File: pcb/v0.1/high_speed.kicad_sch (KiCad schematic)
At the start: 14 parts, among them J1 USB_C_Receptacle_fw, J2 USB_C_Receptacle_fw, J22 690-019-298-412, J5 Conn_01x22_Female, U12 RT9742SNGV, U6 AP22653W6

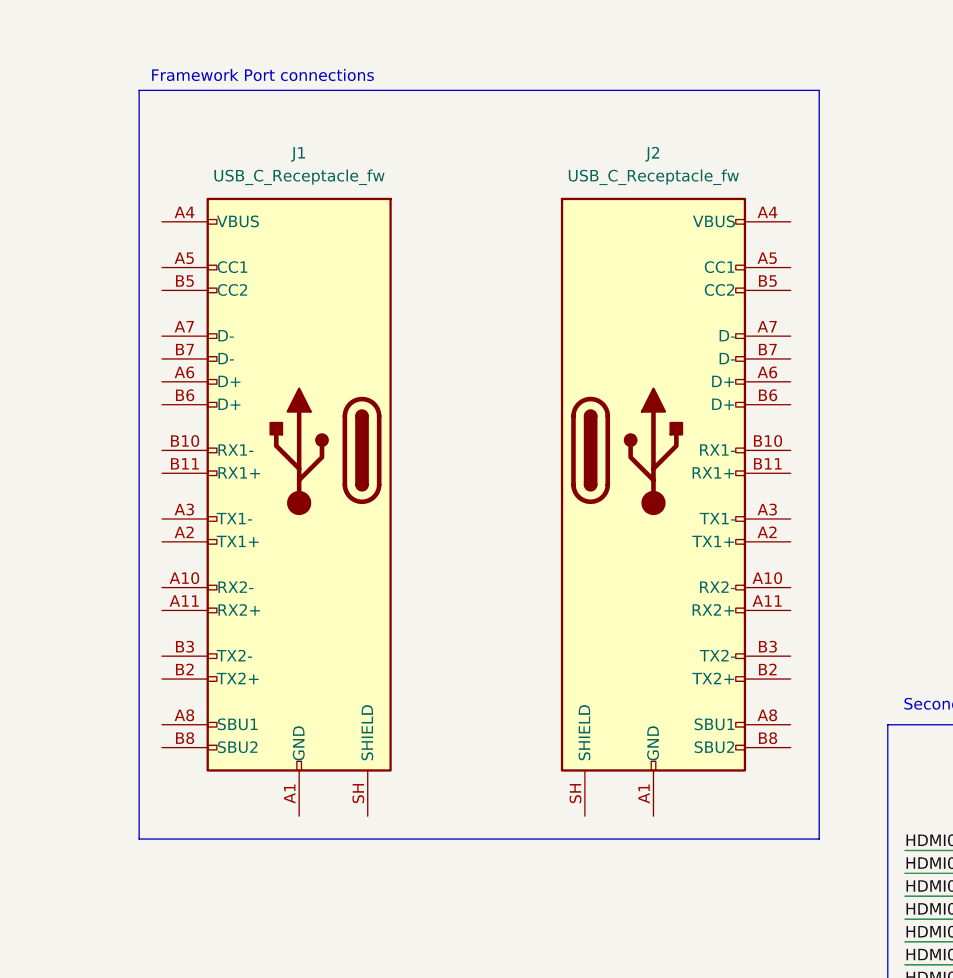
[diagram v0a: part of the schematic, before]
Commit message: Add co processor as its own sub page
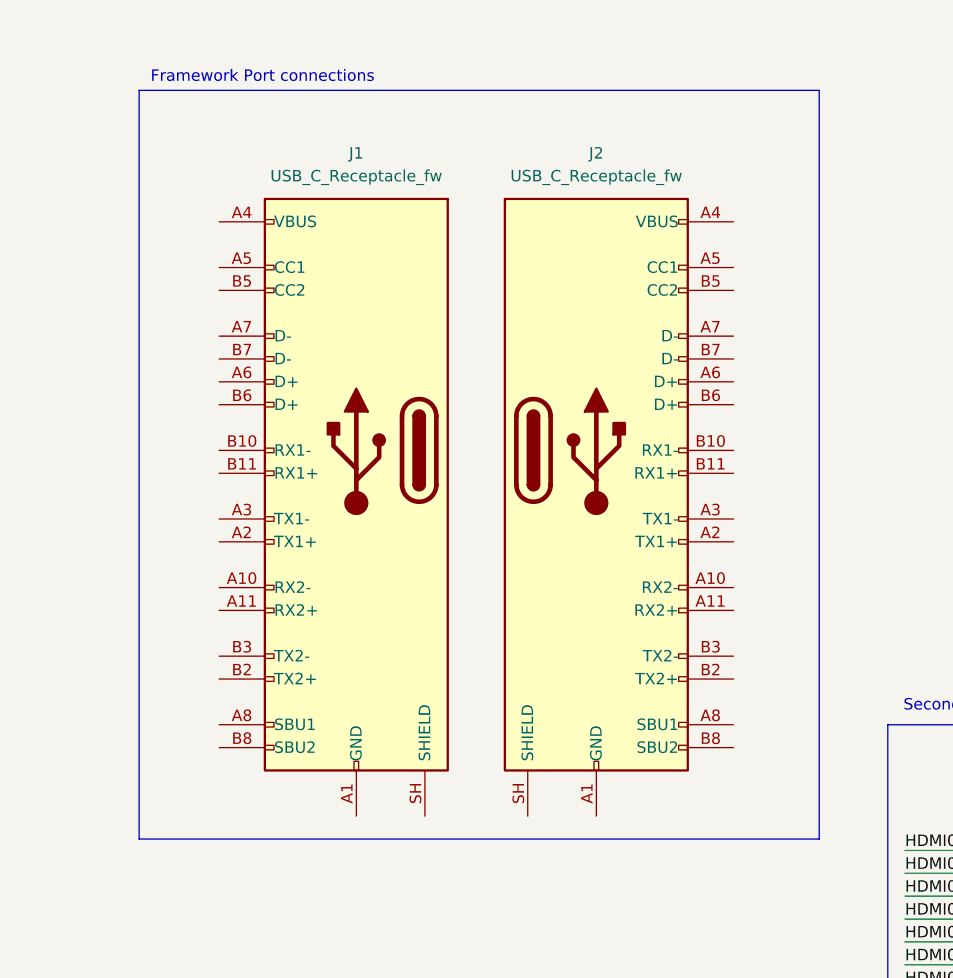
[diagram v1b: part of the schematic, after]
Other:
- moved on the sheet: J1, J2
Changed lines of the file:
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@@
 	(symbol
 		(lib_id "TH-1-CC:USB_C_Receptacle_fw")
-		(at 161.29 60.96 0)
+		(at 167.64 60.96 0)
 		(mirror y)
 		(unit 1)
@@
 		(dnp no)
 		(property "Reference" "J1"
-			(at 161.29 27.94 0)
+			(at 167.64 27.94 0)
 			(show_name no)
 			(do_not_autoplace no)
@@
 		)
 		(property "Value" "USB_C_Receptacle_fw"
-			(at 161.29 30.48 0)
+			(at 167.64 30.48 0)
 			(show_name no)
 			(do_not_autoplace no)
@@
 		)
 		(property "Footprint" ""
-			(at 157.48 60.96 0)
+			(at 163.83 60.96 0)
 			(hide yes)
 			(show_name no)
@@
 		)
 		(property "Datasheet" "https://gct.co/files/specs/usb4056-spec.pdf"
-			(at 157.48 60.96 0)
+			(at 163.83 60.96 0)
 			(hide yes)
 			(show_name no)
@@
 		)
 		(property "Description" "USB Full-Featured Type-C Receptacle connector"
-			(at 161.29 60.96 0)
+			(at 167.64 60.96 0)
 			(hide yes)
 			(show_name no)
@@
 		)
 		(property "Manufacturer" "GCT"
-			(at 161.29 60.96 0)
+			(at 167.64 60.96 0)
 			(hide yes)
 			(show_name no)
@@
 		)
 		(property "Mfr. Part no" "USB4056-03-A"
-			(at 161.29 60.96 0)
+			(at 167.64 60.96 0)
 			(hide yes)
 			(show_name no)
@@
 		)
 		(property "Distributor Digikey" "https://www.digikey.co.uk/en/products/detail/gct/USB4056-03-A/14638038"
-			(at 161.29 60.96 0)
+			(at 167.64 60.96 0)
 			(hide yes)
 			(show_name no)
@@
 		)
 		(property "Digikey Part no" "2073-USB4056-03-ATR-ND"
-			(at 161.29 60.96 0)
+			(at 167.64 60.96 0)
 			(hide yes)
 			(show_name no)
@@
 		)
 		(property "Stock" "NO!"
-			(at 161.29 60.96 0)
+			(at 167.64 60.96 0)
 			(hide yes)
 			(show_name no)
@@
 	(symbol
 		(lib_id "TH-1-CC:USB_C_Receptacle_fw")
-		(at 200.66 60.96 0)
+		(at 194.31 60.96 0)
 		(unit 1)
 		(body_style 1)
@@
 		(fields_autoplaced yes)
 		(property "Reference" "J2"
-			(at 200.66 27.94 0)
+			(at 194.31 27.94 0)
 			(show_name no)
 			(do_not_autoplace no)
@@
 		)
 		(property "Value" "USB_C_Receptacle_fw"
-			(at 200.66 30.48 0)
+			(at 194.31 30.48 0)
 			(show_name no)
 			(do_not_autoplace no)
@@
 		)
 		(property "Footprint" ""
-			(at 204.47 60.96 0)
+			(at 198.12 60.96 0)
 			(hide yes)
 			(show_name no)
@@
 		)
 		(property "Datasheet" "https://gct.co/files/specs/usb4056-spec.pdf"
-			(at 204.47 60.96 0)
+			(at 198.12 60.96 0)
 			(hide yes)
 			(show_name no)
@@
 		)
 		(property "Description" "USB Full-Featured Type-C Receptacle connector"
-			(at 200.66 60.96 0)
+			(at 194.31 60.96 0)
 			(hide yes)
 			(show_name no)
@@
 		)
 		(property "Manufacturer" "GCT"
-			(at 200.66 60.96 0)
+			(at 194.31 60.96 0)
 			(hide yes)
 			(show_name no)
@@
 		)
 		(property "Mfr. Part no" "USB4056-03-A"
-			(at 200.66 60.96 0)
+			(at 194.31 60.96 0)
 			(hide yes)
 			(show_name no)
@@
 		)
 		(property "Distributor Digikey" "https://www.digikey.co.uk/en/products/detail/gct/USB4056-03-A/14638038"
-			(at 200.66 60.96 0)
+			(at 194.31 60.96 0)
 			(hide yes)
 			(show_name no)
@@
 		)
 		(property "Digikey Part no" "2073-USB4056-03-ATR-ND"
-			(at 200.66 60.96 0)
+			(at 194.31 60.96 0)
 			(hide yes)
 			(show_name no)
@@
 		)
 		(property "Stock" "NO!"
-			(at 200.66 60.96 0)
-			(hide yes)
-			(show_name no)
+			(at 194.31 60.96 0)
+			(hide yes)
+			(show_name no)

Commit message: Add IR subsystem to schematic + clean up layout
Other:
- company: (none) -> Teahaz Computer
- title: (none) -> TH-1 Mainbaord devkit: High speed components
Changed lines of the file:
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@@
 	(generator_version "10.0")
 	(paper "A4")
+	(title_block
+		(title "TH-1 Mainbaord devkit: High speed components")
+		(date "2026-05-29")
+		(rev "0.1")
+		(company "Teahaz Computer")
+	)
 	(rectangle
 		(start 143.51 20.955)

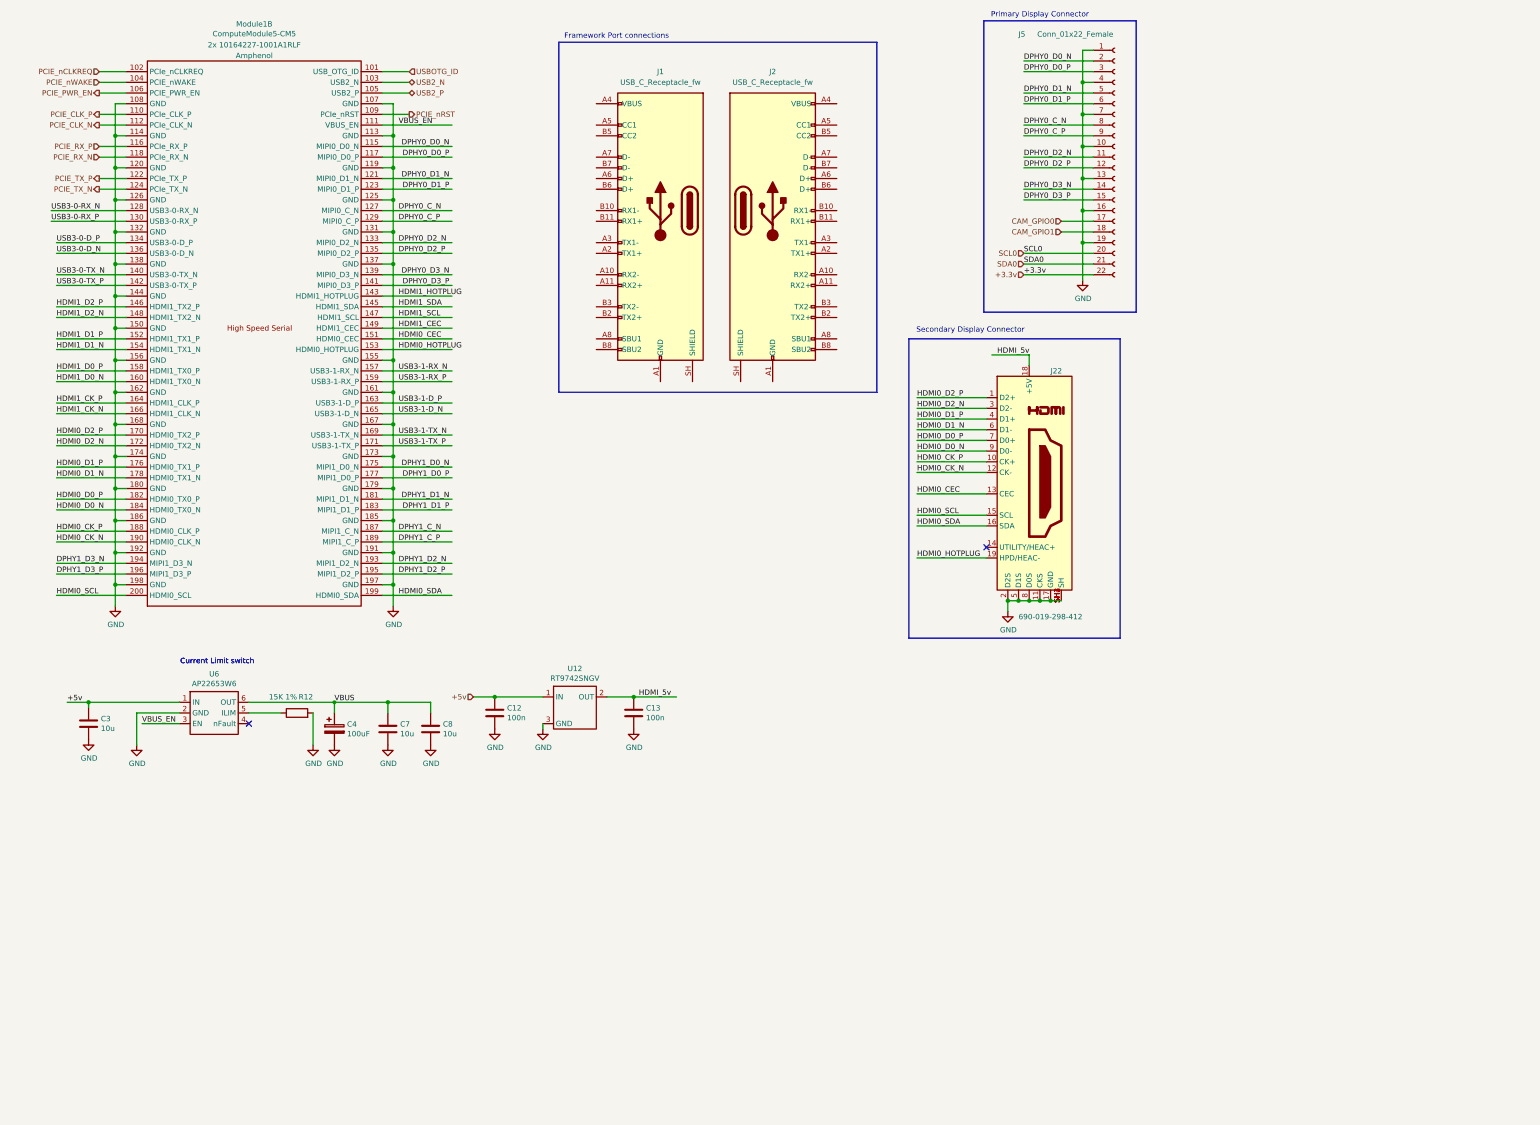
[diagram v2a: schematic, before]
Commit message: More work on the sound system
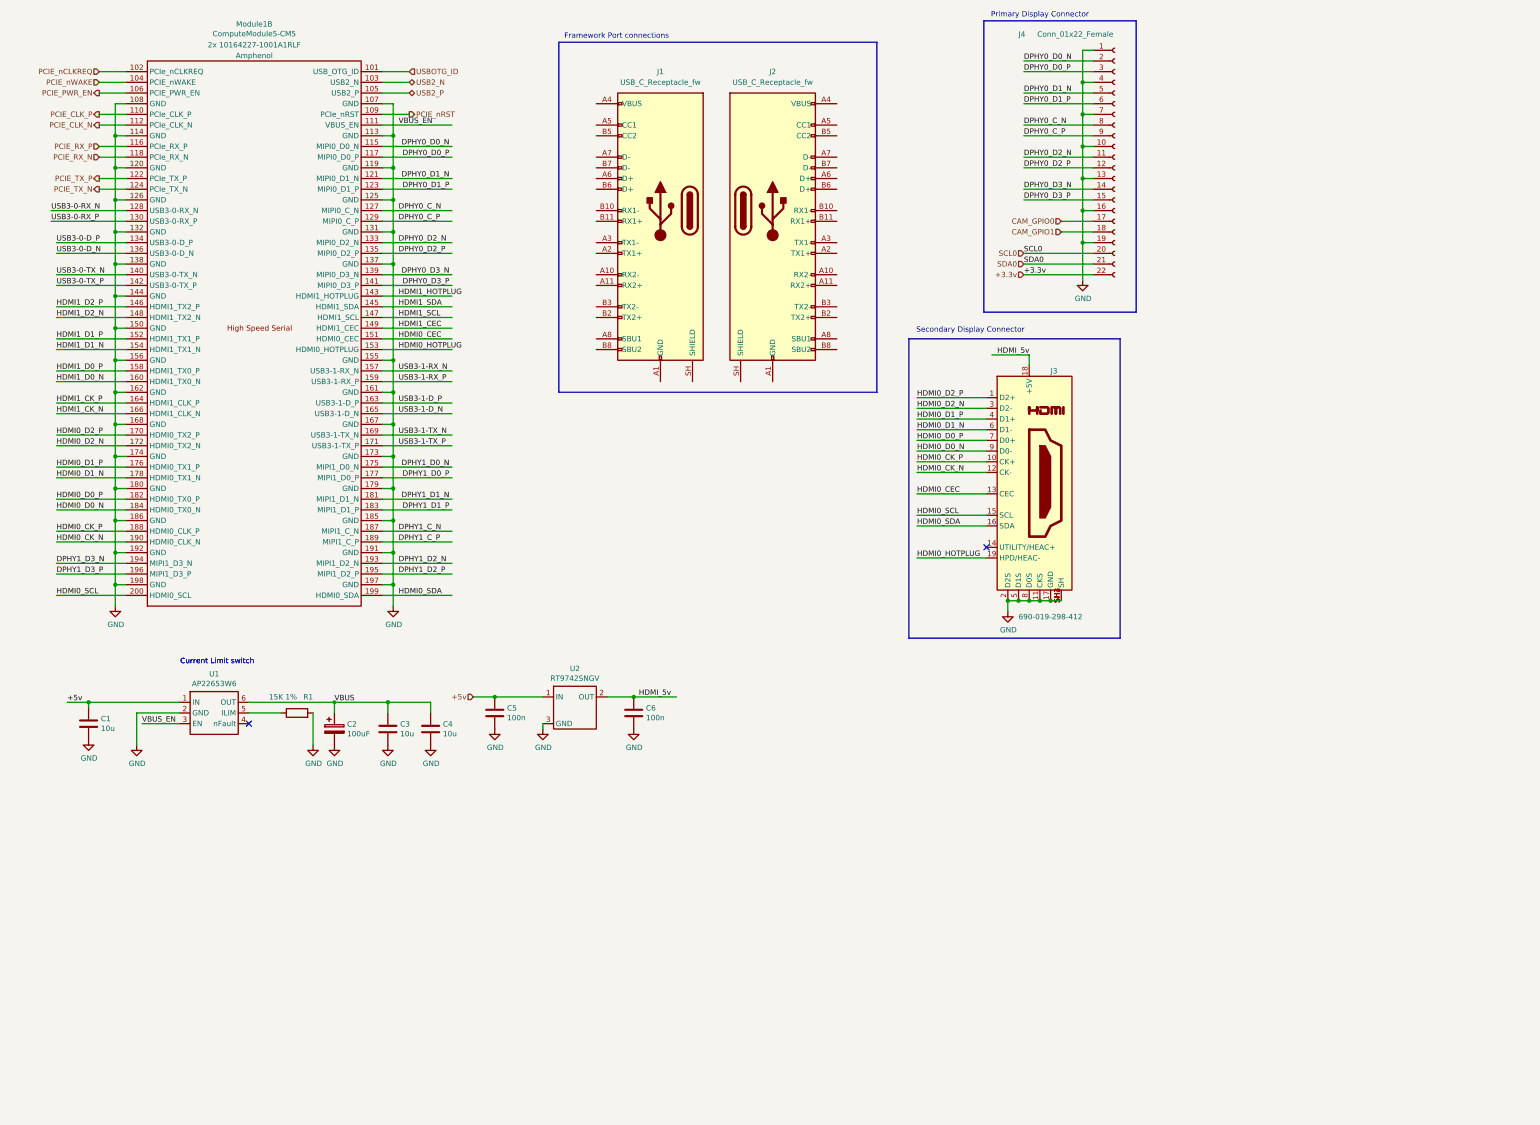
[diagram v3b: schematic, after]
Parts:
- renumbered C3 to C1, C4 to C2, C7 to C3, C8 to C4, C12 to C5, C13 to C6, J22 to J3, J5 to J4, R12 to R1, U6 to U1, U12 to U2
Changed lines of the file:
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@@
 		(in_pos_files yes)
 		(dnp no)
-		(property "Reference" "#PWR010"
+		(property "Reference" "#PWR05"
 			(at 90.17 194.31 0)
 			(hide yes)
@@
 			(project "mainboard"
 				(path "/5b8aa782-5c3d-43e7-a869-3bd000015f52/8e613e76-cfa9-4d70-9fba-6dbea9bbdbc9"
-					(reference "#PWR010")
+					(reference "#PWR05")
 					(unit 1)
 				)
@@
 		(in_pos_files yes)
 		(dnp no)
-		(property "Reference" "#PWR03"
+		(property "Reference" "#PWR01"
 			(at 31.75 193.04 0)
 			(hide yes)
@@
 			(project "mainboard"
 				(path "/5b8aa782-5c3d-43e7-a869-3bd000015f52/8e613e76-cfa9-4d70-9fba-6dbea9bbdbc9"
-					(reference "#PWR03")
+					(reference "#PWR01")
 					(unit 1)
 				)
@@
 		(in_pos_files yes)
 		(dnp no)
-		(property "Reference" "#PWR0138"
+		(property "Reference" "#PWR010"
 			(at 139.7 190.5 0)
 			(hide yes)
@@
 			(project "mainboard"
 				(path "/5b8aa782-5c3d-43e7-a869-3bd000015f52/8e613e76-cfa9-4d70-9fba-6dbea9bbdbc9"
-					(reference "#PWR0138")
+					(reference "#PWR010")
 					(unit 1)
 				)
@@
 		(in_pos_files yes)
 		(dnp no)
-		(property "Reference" "J5"
+		(property "Reference" "J4"
 			(at 252.73 19.05 0)
 			(show_name no)
@@
 			(project "mainboard"
 				(path "/5b8aa782-5c3d-43e7-a869-3bd000015f52/8e613e76-cfa9-4d70-9fba-6dbea9bbdbc9"
-					(reference "J5")
+					(reference "J4")
 					(unit 1)
 				)
@@
 		(in_pos_files yes)
 		(dnp no)
-		(property "Reference" "#PWR07"
+		(property "Reference" "#PWR03"
 			(at 43.18 194.31 0)
 			(hide yes)
@@
 			(project "mainboard"
 				(path "/5b8aa782-5c3d-43e7-a869-3bd000015f52/8e613e76-cfa9-4d70-9fba-6dbea9bbdbc9"
-					(reference "#PWR07")
+					(reference "#PWR03")
 					(unit 1)
 				)
@@
 		(in_pos_files yes)
 		(dnp no)
-		(property "Reference" "C8"
+		(property "Reference" "C4"
 			(at 115.951 182.9816 0)
 			(show_name no)
@@
 			(project "mainboard"
 				(path "/5b8aa782-5c3d-43e7-a869-3bd000015f52/8e613e76-cfa9-4d70-9fba-6dbea9bbdbc9"
-					(reference "C8")
+					(reference "C4")
 					(unit 1)
 				)
@@
 		(in_pos_files yes)
 		(dnp no)
-		(property "Reference" "#PWR012"
+		(property "Reference" "#PWR08"
 			(at 113.03 194.31 0)
 			(hide yes)
@@
 			(project "mainboard"
 				(path "/5b8aa782-5c3d-43e7-a869-3bd000015f52/8e613e76-cfa9-4d70-9fba-6dbea9bbdbc9"
-					(reference "#PWR012")
+					(reference "#PWR08")
 					(unit 1)
 				)
@@
 		(in_pos_files yes)
 		(dnp no)
-		(property "Reference" "#PWR0134"
+		(property "Reference" "#PWR013"
 			(at 267.97 83.82 0)
 			(hide yes)
@@
 			(project "mainboard"
 				(path "/5b8aa782-5c3d-43e7-a869-3bd000015f52/8e613e76-cfa9-4d70-9fba-6dbea9bbdbc9"
-					(reference "#PWR0134")
+					(reference "#PWR013")
 					(unit 1)
 				)
@@
 		(in_pos_files yes)
 		(dnp no)
-		(property "Reference" "U6"
+		(property "Reference" "U1"
 			(at 61.595 171.069 0)
 			(show_name no)
@@
 			(project "mainboard"
 				(path "/5b8aa782-5c3d-43e7-a869-3bd000015f52/8e613e76-cfa9-4d70-9fba-6dbea9bbdbc9"
-					(reference "U6")
+					(reference "U1")
 					(unit 1)
 				)
@@
 		(in_pos_files yes)
 		(dnp no)
-		(property "Reference" "R12"
+		(property "Reference" "R1"
 			(at 85.09 176.53 90)
 			(show_name no)
@@
 			(project "mainboard"
 				(path "/5b8aa782-5c3d-43e7-a869-3bd000015f52/8e613e76-cfa9-4d70-9fba-6dbea9bbdbc9"
-					(reference "R12")
+					(reference "R1")
 					(unit 1)
 				)
@@
 		(in_pos_files yes)
 		(dnp no)
-		(property "Reference" "J22"
+		(property "Reference" "J3"
 			(at 260.35 99.06 0)
 			(show_name no)
@@
 			(project "mainboard"
 				(path "/5b8aa782-5c3d-43e7-a869-3bd000015f52/8e613e76-cfa9-4d70-9fba-6dbea9bbdbc9"
-					(reference "J22")
+					(reference "J3")
 					(unit 1)
 				)
@@
 		(in_pos_files yes)
 		(dnp no)
-		(property "Reference" "C13"
+		(property "Reference" "C6"
 			(at 164.211 179.1716 0)
 			(show_name no)
@@
 			(project "mainboard"
 				(path "/5b8aa782-5c3d-43e7-a869-3bd000015f52/8e613e76-cfa9-4d70-9fba-6dbea9bbdbc9"
-					(reference "C13")
+					(reference "C6")
 					(unit 1)
 				)
@@
 		(in_pos_files yes)
 		(dnp no)
-		(property "Reference" "#PWR0130"
+		(property "Reference" "#PWR07"
 			(at 104.14 161.29 0)
 			(hide yes)
@@
 			(project "mainboard"
 				(path "/5b8aa782-5c3d-43e7-a869-3bd000015f52/8e613e76-cfa9-4d70-9fba-6dbea9bbdbc9"
-					(reference "#PWR0130")
+					(reference "#PWR07")
 					(unit 1)
 				)
@@
 		(in_pos_files yes)
 		(dnp no)
-		(property "Reference" "C3"
+		(property "Reference" "C1"
 			(at 34.671 181.7116 0)
 			(show_name no)
@@
 			(project "mainboard"
 				(path "/5b8aa782-5c3d-43e7-a869-3bd000015f52/8e613e76-cfa9-4d70-9fba-6dbea9bbdbc9"
-					(reference "C3")
+					(reference "C1")
 					(unit 1)
 				)
@@
 		(in_pos_files yes)
 		(dnp no)
-		(property "Reference" "#PWR011"
+		(property "Reference" "#PWR06"
 			(at 102.87 194.31 0)
 			(hide yes)
@@
 			(project "mainboard"
 				(path "/5b8aa782-5c3d-43e7-a869-3bd000015f52/8e613e76-cfa9-4d70-9fba-6dbea9bbdbc9"
-					(reference "#PWR011")
+					(reference "#PWR06")
 					(unit 1)
 				)
@@
 		(in_pos_files yes)
 		(dnp no)
-		(property "Reference" "C12"
+		(property "Reference" "C5"
 			(at 131.191 179.1716 0)
 			(show_name no)
@@
 			(project "mainboard"
 				(path "/5b8aa782-5c3d-43e7-a869-3bd000015f52/8e613e76-cfa9-4d70-9fba-6dbea9bbdbc9"
-					(reference "C12")
+					(reference "C5")
 					(unit 1)
 				)
@@
 		(in_pos_files yes)
 		(dnp no)
-		(property "Reference" "U12"
+		(property "Reference" "U2"
 			(at 147.32 169.799 0)
 			(show_name no)
@@
 			(project "mainboard"
 				(path "/5b8aa782-5c3d-43e7-a869-3bd000015f52/8e613e76-cfa9-4d70-9fba-6dbea9bbdbc9"
-					(reference "U12")
+					(reference "U2")
 					(unit 1)
 				)
@@
 		(in_pos_files yes)
 		(dnp no)
-		(property "Reference" "#PWR09"
+		(property "Reference" "#PWR04"
 			(at 85.09 194.31 0)
 			(hide yes)
@@
 			(project "mainboard"
 				(path "/5b8aa782-5c3d-43e7-a869-3bd000015f52/8e613e76-cfa9-4d70-9fba-6dbea9bbdbc9"
-					(reference "#PWR09")
+					(reference "#PWR04")
 					(unit 1)
 				)
@@
 		(in_pos_files yes)
 		(dnp no)
-		(property "Reference" "#PWR0128"
+		(property "Reference" "#PWR012"
 			(at 250.19 162.56 0)
 			(hide yes)
@@
 			(project "mainboard"
 				(path "/5b8aa782-5c3d-43e7-a869-3bd000015f52/8e613e76-cfa9-4d70-9fba-6dbea9bbdbc9"
-					(reference "#PWR0128")
+					(reference "#PWR012")
 					(unit 1)
 				)
@@
 		(in_pos_files yes)
 		(dnp no)
-		(property "Reference" "C4"
+		(property "Reference" "C2"
 			(at 93.1672 183.007 0)
 			(show_name no)
@@
 			(project "mainboard"
 				(path "/5b8aa782-5c3d-43e7-a869-3bd000015f52/8e613e76-cfa9-4d70-9fba-6dbea9bbdbc9"
-					(reference "C4")
+					(reference "C2")
 					(unit 1)
 				)
@@
 		(in_pos_files yes)
 		(dnp no)
-		(property "Reference" "#PWR0137"
+		(property "Reference" "#PWR09"
 			(at 128.27 190.5 0)
 			(hide yes)
@@
 			(project "mainboard"
 				(path "/5b8aa782-5c3d-43e7-a869-3bd000015f52/8e613e76-cfa9-4d70-9fba-6dbea9bbdbc9"
-					(reference "#PWR0137")
+					(reference "#PWR09")
 					(unit 1)
 				)
@@
 		(in_pos_files yes)
 		(dnp no)
-		(property "Reference" "#PWR0136"
+		(property "Reference" "#PWR011"
 			(at 161.29 190.5 0)
 			(hide yes)
@@
 			(project "mainboard"
 				(path "/5b8aa782-5c3d-43e7-a869-3bd000015f52/8e613e76-cfa9-4d70-9fba-6dbea9bbdbc9"
-					(reference "#PWR0136")
+					(reference "#PWR011")
 					(unit 1)
 				)
@@
 		(in_pos_files yes)
 		(dnp no)
-		(property "Reference" "C7"
+		(property "Reference" "C3"
 			(at 105.791 182.9816 0)
 			(show_name no)
@@
 			(project "mainboard"
 				(path "/5b8aa782-5c3d-43e7-a869-3bd000015f52/8e613e76-cfa9-4d70-9fba-6dbea9bbdbc9"
-					(reference "C7")
+					(reference "C3")
 					(unit 1)
 				)
@@
 		(in_pos_files yes)
 		(dnp no)
-		(property "Reference" "#PWR0131"
+		(property "Reference" "#PWR02"
 			(at 38.1 161.29 0)
 			(hide yes)
@@
 			(project "mainboard"
 				(path "/5b8aa782-5c3d-43e7-a869-3bd000015f52/8e613e76-cfa9-4d70-9fba-6dbea9bbdbc9"
-					(reference "#PWR0131")
+					(reference "#PWR02")
 					(unit 1)
 				)
